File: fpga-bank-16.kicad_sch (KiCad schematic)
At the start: 3 parts, among them U4 XC7K160T-FFG676, Y3 Oscillator_100MHz_ASFL1

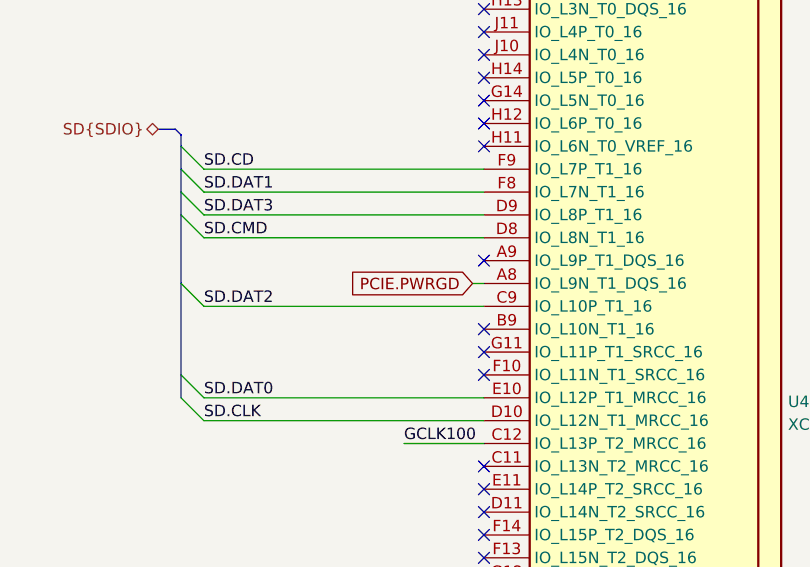
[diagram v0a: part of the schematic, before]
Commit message: Removing PCIe from sch and PCB
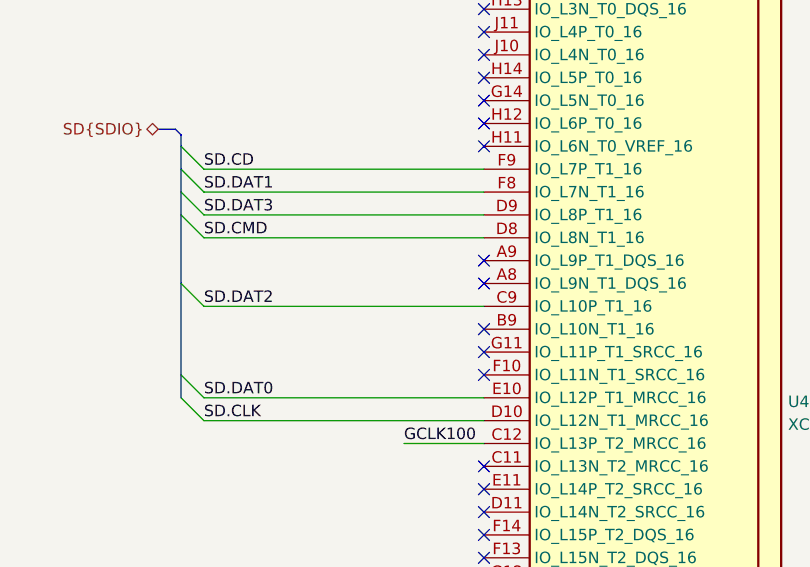
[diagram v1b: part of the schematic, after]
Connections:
- net PCIE.PWRGD: no longer names the net of U4.A8 (IO_L9N_T1_DQS_16)
- no-connect marks 33 -> 34
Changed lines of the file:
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@@
   (no_connect (at 185.42 166.37))
   (no_connect (at 185.42 133.35))
+  (no_connect (at 185.42 123.19))
   (no_connect (at 185.42 163.83))
   (no_connect (at 185.42 120.65))
@@
     (stroke (width 0) (type default))
   )
-  (wire (pts (xy 184.15 123.19) (xy 185.42 123.19))
-    (stroke (width 0) (type default))
-  )
   (wire (pts (xy 34.925 257.81) (xy 36.83 257.81))
     (stroke (width 0) (type default))
@@
     (effects (font (size 1.27 1.27)) (justify left bottom))
   )
-  (global_label "PCIE.PWRGD" (shape input) (at 184.15 123.19 180) (fields_autoplaced)
-    (effects (font (size 1.27 1.27)) (justify right))
-    (property "Intersheetrefs" "${INTERSHEET_REFS}" (at 170.3958 123.2694 0)
-      (effects (font (size 1.27 1.27)) (justify right))
-    )
-  )
   (hierarchical_label "SD{SDIO}" (shape bidirectional) (at 149.225 106.045 180) (fields_autoplaced)

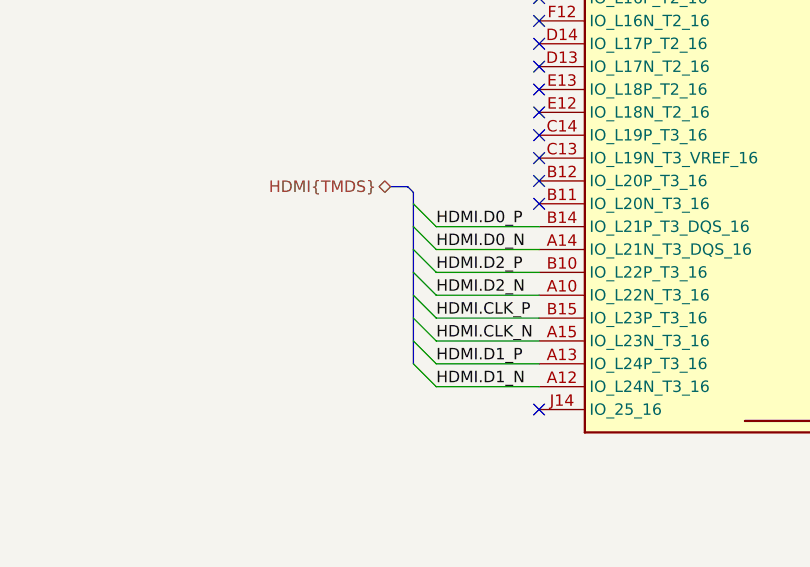
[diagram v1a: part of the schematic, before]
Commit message: Removing HDMI from sch and PCB
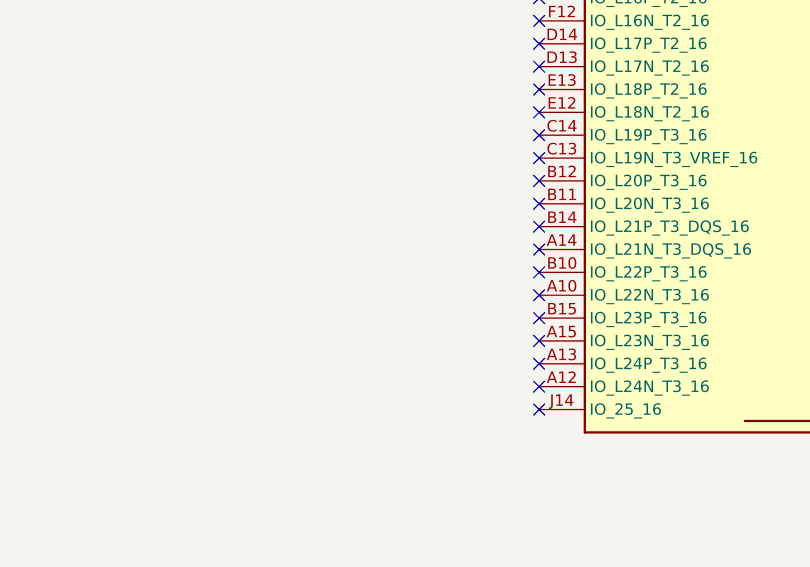
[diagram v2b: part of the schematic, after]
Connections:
- net HDMI.CLK_N: no longer names the net of U4.A15 (IO_L23N_T3_16)
- net HDMI.CLK_P: no longer names the net of U4.B15 (IO_L23P_T3_16)
- net HDMI.D0_N: no longer names the net of U4.A14 (IO_L21N_T3_DQS_16)
- net HDMI.D0_P: no longer names the net of U4.B14 (IO_L21P_T3_DQS_16)
- net HDMI.D1_N: no longer names the net of U4.A12 (IO_L24N_T3_16)
- net HDMI.D1_P: no longer names the net of U4.A13 (IO_L24P_T3_16)
- net HDMI.D2_N: no longer names the net of U4.A10 (IO_L22N_T3_16)
- net HDMI.D2_P: no longer names the net of U4.B10 (IO_L22P_T3_16)
- no-connect marks 34 -> 42
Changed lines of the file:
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@@
   (no_connect (at 185.42 161.29))
   (no_connect (at 185.42 156.21))
+  (no_connect (at 185.42 196.85))
   (no_connect (at 185.42 176.53))
   (no_connect (at 185.42 100.33))
+  (no_connect (at 185.42 189.23))
   (no_connect (at 185.42 168.91))
   (no_connect (at 185.42 151.13))
   (no_connect (at 185.42 166.37))
+  (no_connect (at 185.42 181.61))
   (no_connect (at 185.42 133.35))
   (no_connect (at 185.42 123.19))
   (no_connect (at 185.42 163.83))
   (no_connect (at 185.42 120.65))
+  (no_connect (at 185.42 184.15))
+  (no_connect (at 185.42 186.69))
   (no_connect (at 185.42 179.07))
+  (no_connect (at 185.42 199.39))
+  (no_connect (at 185.42 194.31))
   (no_connect (at 185.42 158.75))
   (no_connect (at 185.42 77.47))
+  (no_connect (at 185.42 191.77))
   (no_connect (at 185.42 153.67))
   (no_connect (at 185.42 148.59))
@@
     (stroke (width 0) (type default))
   )
-  (bus_entry (at 173.99 184.15) (size -2.54 -2.54)
-    (stroke (width 0) (type default))
-  )
   (bus_entry (at 154.305 125.73) (size -2.54 -2.54)
-    (stroke (width 0) (type default))
-  )
-  (bus_entry (at 173.99 196.85) (size -2.54 -2.54)
-    (stroke (width 0) (type default))
-  )
-  (bus_entry (at 173.99 186.69) (size -2.54 -2.54)
     (stroke (width 0) (type default))
   )
@@
     (stroke (width 0) (type default))
   )
-  (bus_entry (at 173.99 194.31) (size -2.54 -2.54)
-    (stroke (width 0) (type default))
-  )
   (bus_entry (at 154.305 138.43) (size -2.54 -2.54)
     (stroke (width 0) (type default))
   )
-  (bus_entry (at 173.99 189.23) (size -2.54 -2.54)
-    (stroke (width 0) (type default))
-  )
   (bus_entry (at 154.305 113.03) (size -2.54 -2.54)
-    (stroke (width 0) (type default))
-  )
-  (bus_entry (at 173.99 181.61) (size -2.54 -2.54)
-    (stroke (width 0) (type default))
-  )
-  (bus_entry (at 173.99 191.77) (size -2.54 -2.54)
-    (stroke (width 0) (type default))
-  )
-  (bus_entry (at 173.99 199.39) (size -2.54 -2.54)
     (stroke (width 0) (type default))
   )
@@
     (stroke (width 0) (type default))
   )
-  (bus (pts (xy 171.45 177.8) (xy 171.45 179.07))
-    (stroke (width 0) (type default))
-  )
-  (bus (pts (xy 171.45 194.31) (xy 171.45 196.85))
-    (stroke (width 0) (type default))
-  )
-  (bus (pts (xy 171.45 186.69) (xy 171.45 189.23))
-    (stroke (width 0) (type default))
-  )
   (bus (pts (xy 151.765 115.57) (xy 151.765 123.19))
     (stroke (width 0) (type default))
@@
     (stroke (width 0) (type default))
   )
-  (bus (pts (xy 168.91 177.165) (xy 170.815 177.165))
-    (stroke (width 0) (type default))
-  )
-  (bus (pts (xy 170.815 177.165) (xy 171.45 177.8))
-    (stroke (width 0) (type default))
-  )
-  (wire (pts (xy 185.42 189.23) (xy 173.99 189.23))
-    (stroke (width 0) (type default))
-  )
   (bus (pts (xy 151.765 123.19) (xy 151.765 133.35))
     (stroke (width 0) (type default))
   )
   (wire (pts (xy 26.035 267.335) (xy 26.035 264.795))
-    (stroke (width 0) (type default))
-  )
-  (wire (pts (xy 185.42 186.69) (xy 173.99 186.69))
     (stroke (width 0) (type default))
   )
@@
     (stroke (width 0) (type default))
   )
-  (bus (pts (xy 171.45 191.77) (xy 171.45 194.31))
-    (stroke (width 0) (type default))
-  )
   (bus (pts (xy 151.765 110.49) (xy 151.765 113.03))
     (stroke (width 0) (type default))
@@
     (stroke (width 0) (type default))
   )
-  (bus (pts (xy 171.45 189.23) (xy 171.45 191.77))
-    (stroke (width 0) (type default))
-  )
   (wire (pts (xy 26.035 257.81) (xy 34.925 257.81))
-    (stroke (width 0) (type default))
-  )
-  (bus (pts (xy 171.45 181.61) (xy 171.45 184.15))
-    (stroke (width 0) (type default))
-  )
-  (wire (pts (xy 185.42 181.61) (xy 173.99 181.61))
     (stroke (width 0) (type default))
   )
@@
     (stroke (width 0) (type default))
   )
-  (wire (pts (xy 185.42 196.85) (xy 173.99 196.85))
-    (stroke (width 0) (type default))
-  )
   (wire (pts (xy 154.305 125.73) (xy 185.42 125.73))
-    (stroke (width 0) (type default))
-  )
-  (wire (pts (xy 185.42 194.31) (xy 173.99 194.31))
     (stroke (width 0) (type default))
   )
@@
   )
   (wire (pts (xy 26.035 259.715) (xy 26.035 257.81))
-    (stroke (width 0) (type default))
-  )
-  (bus (pts (xy 171.45 179.07) (xy 171.45 181.61))
     (stroke (width 0) (type default))
   )
@@
     (stroke (width 0) (type default))
   )
-  (wire (pts (xy 185.42 184.15) (xy 173.99 184.15))
-    (stroke (width 0) (type default))
-  )
   (wire (pts (xy 154.305 118.11) (xy 185.42 118.11))
-    (stroke (width 0) (type default))
-  )
-  (wire (pts (xy 185.42 191.77) (xy 173.99 191.77))
     (stroke (width 0) (type default))
   )
@@
   )
   (wire (pts (xy 55.88 257.81) (xy 65.405 257.81))
-    (stroke (width 0) (type default))
-  )
-  (bus (pts (xy 171.45 184.15) (xy 171.45 186.69))
-    (stroke (width 0) (type default))
-  )
-  (wire (pts (xy 185.42 199.39) (xy 173.99 199.39))
     (stroke (width 0) (type default))
   )
@@
     (effects (font (size 1.27 1.27)) (justify right bottom))
   )
-  (label "HDMI.D2_P" (at 173.99 186.69 0) (fields_autoplaced)
-    (effects (font (size 1.27 1.27)) (justify left bottom))
-  )
-  (label "HDMI.D2_N" (at 173.99 189.23 0) (fields_autoplaced)
-    (effects (font (size 1.27 1.27)) (justify left bottom))
-  )
   (label "SD.DAT3" (at 154.305 115.57 0) (fields_autoplaced)
-    (effects (font (size 1.27 1.27)) (justify left bottom))
-  )
-  (label "HDMI.CLK_N" (at 173.99 194.31 0) (fields_autoplaced)
-    (effects (font (size 1.27 1.27)) (justify left bottom))
-  )
-  (label "HDMI.CLK_P" (at 173.99 191.77 0) (fields_autoplaced)
-    (effects (font (size 1.27 1.27)) (justify left bottom))
-  )
-  (label "HDMI.D0_P" (at 173.99 181.61 0) (fields_autoplaced)
-    (effects (font (size 1.27 1.27)) (justify left bottom))
-  )
-  (label "HDMI.D0_N" (at 173.99 184.15 0) (fields_autoplaced)
-    (effects (font (size 1.27 1.27)) (justify left bottom))
-  )
-  (label "HDMI.D1_P" (at 173.99 196.85 0) (fields_autoplaced)
     (effects (font (size 1.27 1.27)) (justify left bottom))
   )
@@
     (effects (font (size 1.27 1.27)) (justify left bottom))
   )
-  (label "HDMI.D1_N" (at 173.99 199.39 0) (fields_autoplaced)
-    (effects (font (size 1.27 1.27)) (justify left bottom))
-  )
   (hierarchical_label "SD{SDIO}" (shape bidirectional) (at 149.225 106.045 180) (fields_autoplaced)
     (effects (font (size 1.27 1.27)) (justify right))
   )
-  (hierarchical_label "HDMI{TMDS}" (shape bidirectional) (at 168.91 177.165 180) (fields_autoplaced)
-    (effects (font (size 1.27 1.27)) (justify right))
-  )
